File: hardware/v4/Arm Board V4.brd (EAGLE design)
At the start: 114.3 x 50.8 mm, 51 parts, among them IC3 L6206D, U1 SN74LS241DW, U2 XBEE-1B3, U3 LSM9DS0

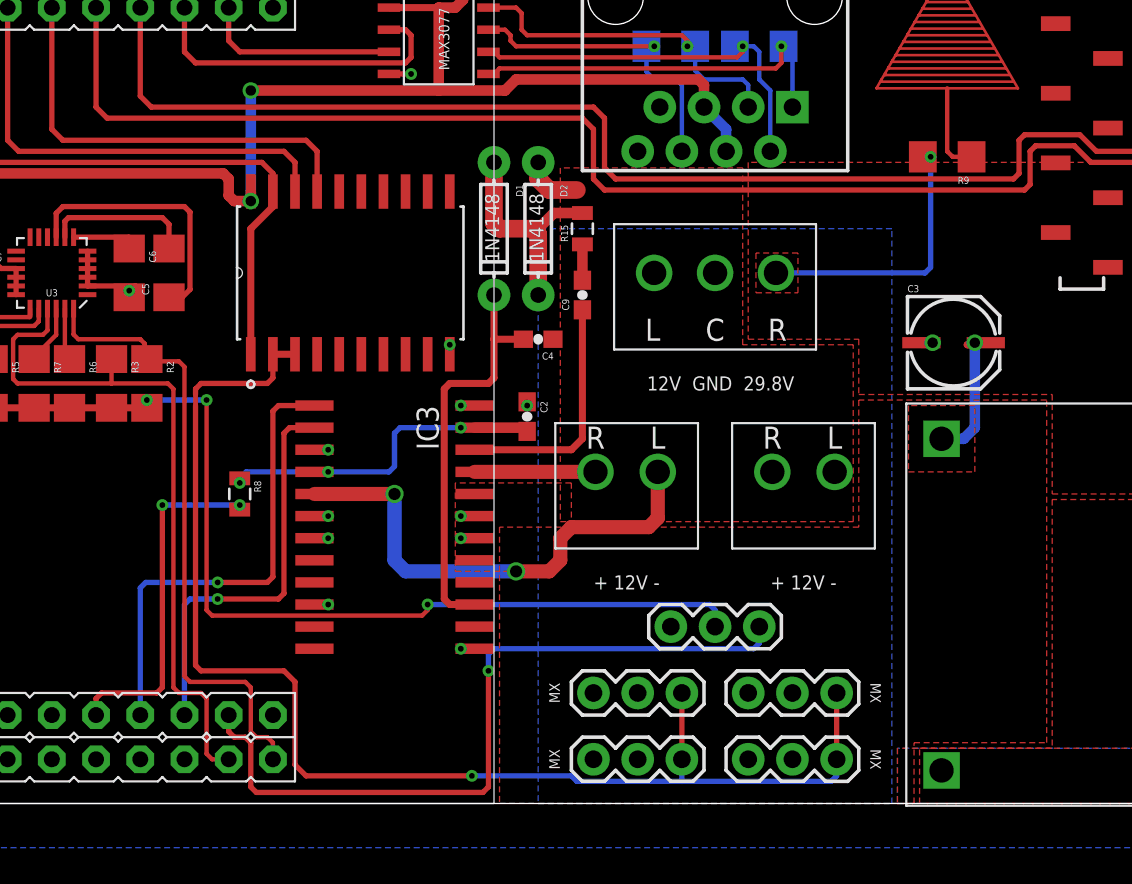
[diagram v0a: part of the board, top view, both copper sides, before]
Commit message: Added motor controller and cleaned it up
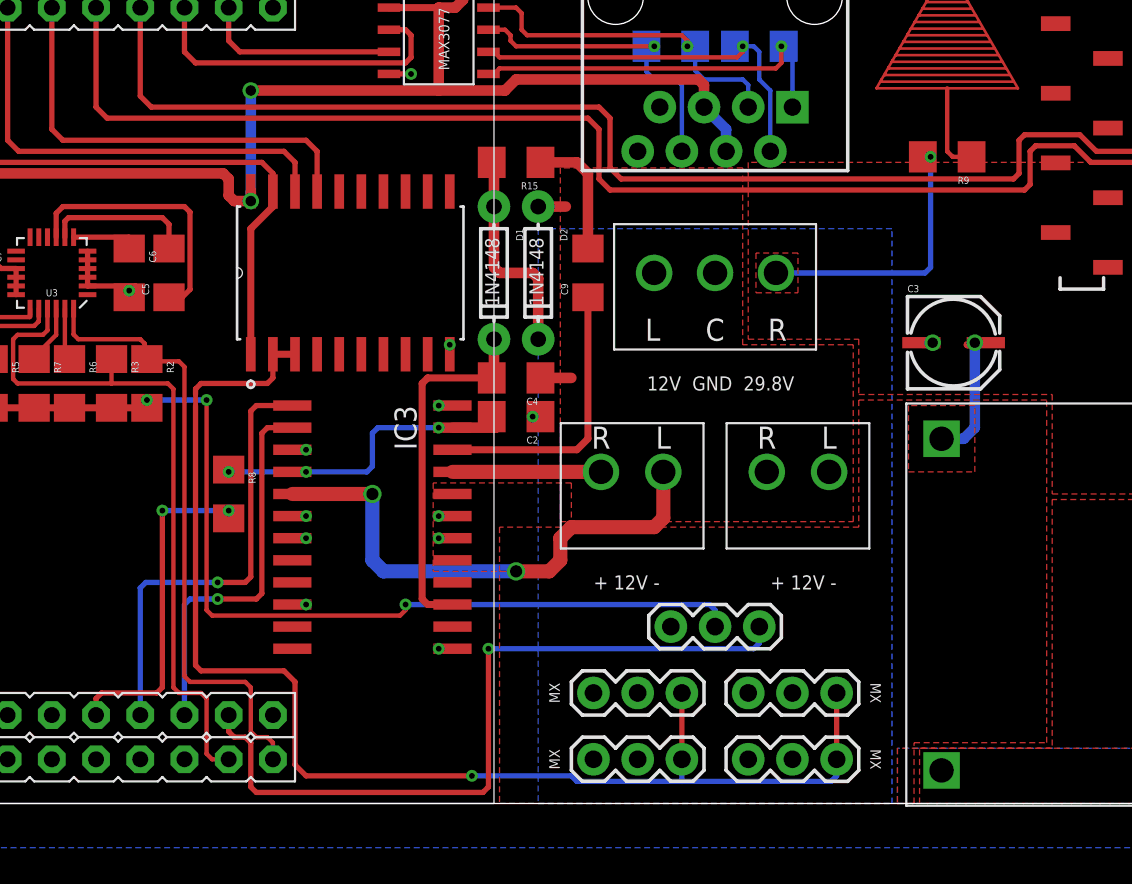
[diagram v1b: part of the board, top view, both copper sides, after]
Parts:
- C2, C4, C9: device SparkFun-Capacitors:0603-CAP -> SparkFun-Passives:1206
- R15, R8: device SparkFun-Passives:0805 -> SparkFun-Resistors:1206
- moved R15 5.39 mm to (45.7, 36.8), turned to 180 degrees
- moved C4 2.56 mm to (45.7, 24.4)
- moved D1 2.54 mm to (44.5, 30.5)
- moved D2 2.54 mm to (47.0, 30.5)
- moved C9 1.31 mm to (49.8, 30.5)
- moved IC3 1.27 mm to (37.5, 15.9)
- moved C2 0.63 mm to (45.7, 22.2), turned to 180 degrees
- moved R8 0.63 mm to (29.2, 17.8)
- moved U$6 0.32 mm to (52.4, 19.1)
- moved U$7 0.32 mm to (61.9, 19.1)
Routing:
- net N$18: track 2.06 -> 7.65 mm
- net VBOOT: track 23.5 -> 20.8 mm
- net N$19: track 13.9 -> 16.2 mm
- net A2: track 6.95 -> 8.53 mm
- net A1: track 28.5 -> 30.1 mm
- net IN1_A: track 27.2 -> 26.0 mm
- net IN2_A: track 23.4 -> 22.1 mm
- net OCD_A: track 20.2 -> 19.2 mm
- net EN_A: track 20.2 -> 19.4 mm
- net N$17: track 13.0 -> 12.5 mm

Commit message: Clean up. Clean up. Clean up everywhere!
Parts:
- moved C2 23.9 mm to (22.2, 18.1), turned to 90 degrees
- moved R8 4.77 mm to (24.4, 18.1)
- moved D2 3.49 mm to (43.5, 30.5)
- moved C4 3.33 mm to (42.4, 24.4)
- moved R15 3.33 mm to (42.4, 36.8)
- moved D1 3.18 mm to (41.3, 30.5)
- moved C9 3.02 mm to (46.8, 30.5)
- moved U1 2.54 mm to (33.7, 30.5)
- moved IC3 2.22 mm to (35.2, 15.9)
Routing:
- net +5V: track 116.1 -> 142.8 mm, vias 2 -> 0
- net +3V3: track 275.7 -> 292.0 mm, vias 7 -> 5
- net A1: track 30.1 -> 25.4 mm, vias 2 -> 1
- net EN_A: track 19.4 -> 15.0 mm, vias 2 -> 0
- net RX_1: track 26.3 -> 23.8 mm
- net TX_1: track 25.1 -> 22.5 mm
- net DC_1: track 37.5 -> 34.9 mm
- net A2: track 8.53 -> 10.8 mm
- net IN1_A: track 26.0 -> 23.9 mm
- net IN2_A: track 22.1 -> 20.1 mm
- net OCD_A: track 19.2 -> 21.2 mm
- net DDATA_1: track 76.1 -> 74.4 mm
- net GND: track 18.3 -> 19.2 mm
- net N$19: track 16.2 -> 15.4 mm
- net VBOOT: track 20.8 -> 20.2 mm

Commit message: Stuff
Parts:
- moved C5 2.54 mm to (23.2, 30.5)
- moved C6 2.38 mm to (21.1, 30.5)
- moved U3 2.06 mm to (17.0, 30.5)
- moved R4 2.06 mm to (11.5, 24.1)
- moved R5 2.06 mm to (13.6, 24.1)
- moved R2 2.06 mm to (22.4, 24.1)
- moved R3 2.06 mm to (20.4, 24.1)
- moved R6 2.06 mm to (18.0, 24.1)
- moved R7 2.06 mm to (16.0, 24.1)
- moved R8 1.91 mm to (22.5, 18.1)
- moved C2 1.75 mm to (20.5, 18.1)
- moved IC3 1.59 mm to (33.7, 15.9)
- moved C7 1.43 mm to (13.2, 30.5)
- moved C8 1.27 mm to (10.8, 30.5)
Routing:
- net +3V3: track 292.0 -> 306.1 mm, vias 5 -> 3
- net VIN: track 16.0 -> 3.30 mm, vias 1 -> 2
- net DDATA_1: track 74.4 -> 77.6 mm
- net LA_ENC: track 43.5 -> 46.4 mm
- net SDA: track 36.1 -> 38.5 mm
- net SCL: track 40.4 -> 42.5 mm
- net VBOOT: track 20.2 -> 21.7 mm
- net N$19: track 15.4 -> 17.0 mm
- net IN1_A: track 23.9 -> 22.3 mm
- net A2: track 10.8 -> 12.3 mm
- net A1: track 25.4 -> 27.0 mm
- net EN_A: track 15.0 -> 13.6 mm
- net IN2_A: track 20.1 -> 18.7 mm
- net GND: track 19.2 -> 17.9 mm
- net DC_1: track 34.9 -> 35.9 mm
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
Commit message: A few finishing things
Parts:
- C1: value .1uF -> (none); device SparkFun-Capacitors:1206 -> SparkFun-Passives:PANASONIC_C
- moved C1 1.93 mm to (110.5, 17.5), turned to 90 degrees
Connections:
- net GND: now also C1.-; no longer C1.2
- net VIN: now also C1.+; no longer C1.1
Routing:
- net +5V: track 142.4 -> 146.7 mm
- net +3V3: track 306.1 -> 303.6 mm
